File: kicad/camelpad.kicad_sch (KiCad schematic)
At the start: 33 parts, among them J1 USB_C_Receptacle_USB2.0_16P, J3 Molex PicoBlade 533980471, SW1 SWITCH_PUSHBUTTON_KAILH_SOCKET, SW2 SWITCH_PUSHBUTTON_KAILH_SOCKET, SW3 SWITCH_PUSHBUTTON_KAILH_SOCKET, SW4 SWITCH_PUSHBUTTON_KAILH_SOCKET, SW5 SWITCH_PUSHBUTTON_KAILH_SOCKET, SW6 SWITCH_PUSHBUTTON_KAILH_SOCKET, U1 ATtiny816-M, U2 AP2127K-3.3

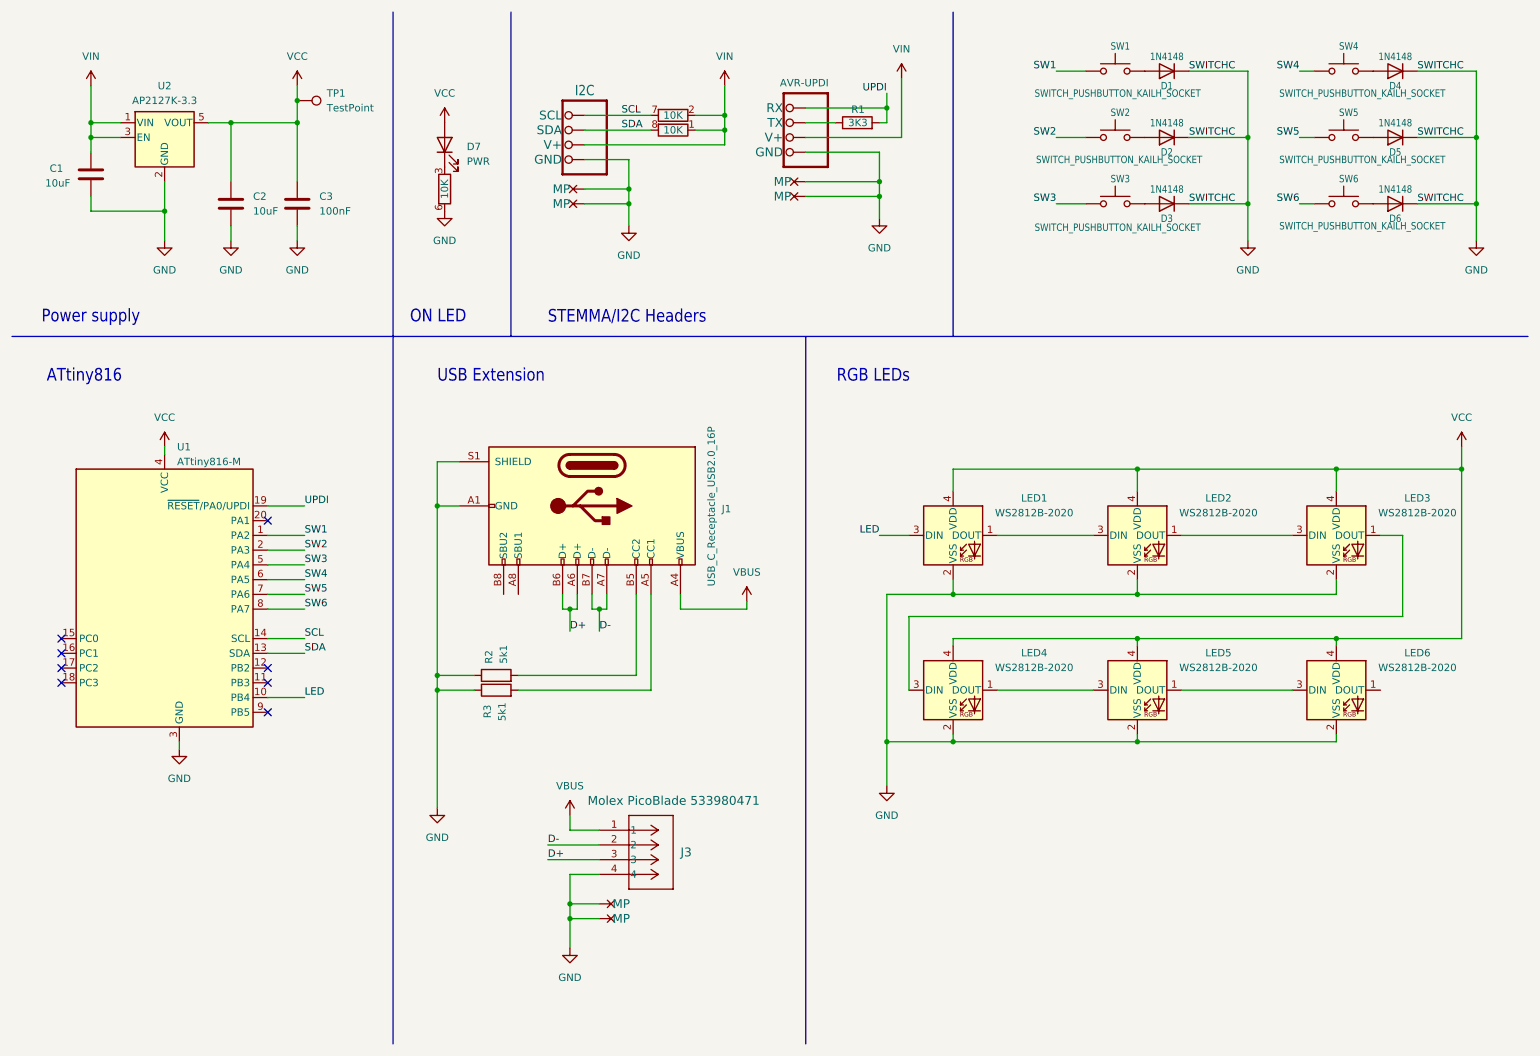
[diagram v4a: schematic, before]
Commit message: Remove LDO as it's not needed. Clean 3v3 power comes from the controller
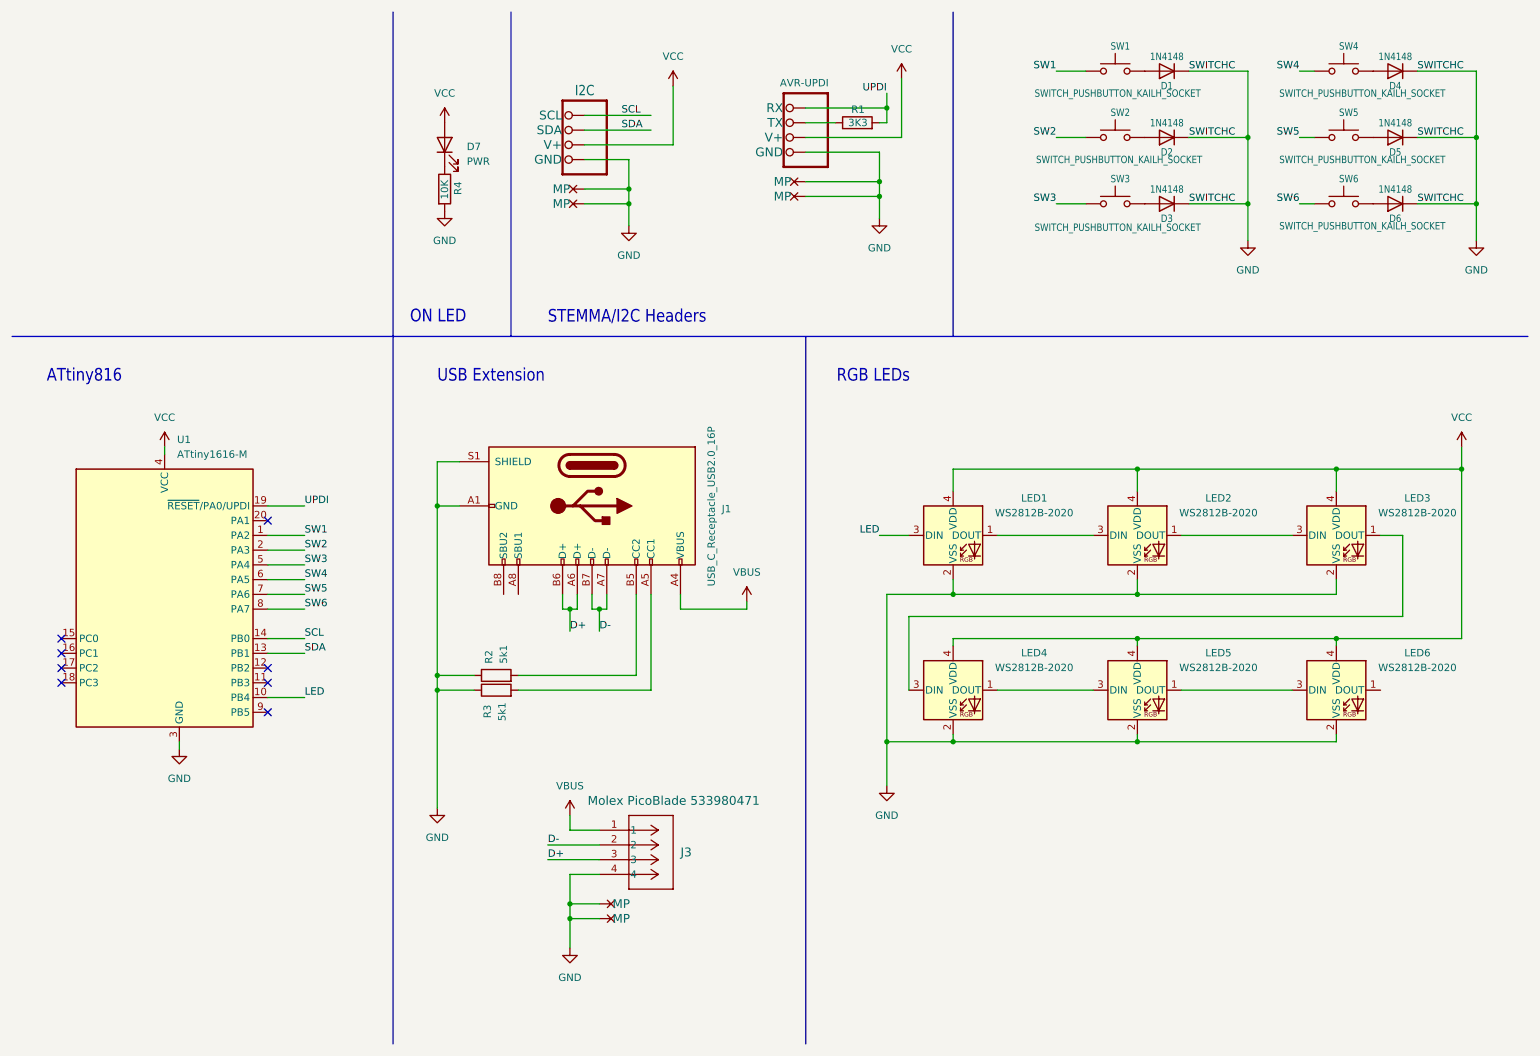
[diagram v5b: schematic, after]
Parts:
- removed C1, C2: 10uF, camelpad:C_0603_1608Metric, symbol Device:C
- removed C3: 100nF, camelpad:C_0603_1608Metric, symbol Device:C
- removed RN1: 10K, camelpad:R_Array_Convex_4x1206, symbol Device:R_Pack04_Split
- removed TP1: TestPoint, TestPoint:TestPoint_Pad_D1.0mm, symbol Connector:TestPoint
- removed U2: AP2127K-3.3, Package_TO_SOT_SMD:SOT-23-5, symbol Regulator_Linear:AP2127K-3.3
- added R4: 10K, camelpad:R0603, symbol Device:R
- D1, D2, D3, D4, D5, D6: footprint camelpad:D_SOD-323 -> camelpad:SOD-323_L1.8-W1.3-LS2.5-RD
- R1, R2, R3: footprint camelpad:R_0603_1608Metric -> camelpad:R0603
- U1: value ATtiny816-M -> ATtiny1616-M; footprint camelpad:VQFN-20-1EP_3x3mm_P0.4mm_EP1.7x1.7mm -> camelpad:QFN-20_L3.0-W3.0-P0.40-BL-EP1.7; symbol camelpad:ATtiny816-M -> camelpad:ATtiny1616-M
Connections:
- net VIN is gone; now on net VCC: I2C1.2 (V+), UPDI1.2 (V+)
- net GND: now also R4.2
- net at D7.1 (K): now also R4.1
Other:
- note removed: "Power supply"
